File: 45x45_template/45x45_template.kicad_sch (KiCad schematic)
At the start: 10 parts, among them J1 Screw_Terminal_01x02

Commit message: Updated template.
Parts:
- removed J1: Screw_Terminal_01x02, TerminalBlock_Phoenix:TerminalBlock_Phoenix_MKDS-1,5-2-5.08_1x02_P5.08mm_Horizontal, symbol Connector:Screw_Terminal_01x02
- removed R3, R4: 100k, Resistor_THT:R_Axial_DIN0207_L6.3mm_D2.5mm_P15.24mm_Horizontal, symbol Device:R
- removed V1: VPULSE, symbol Simulation_SPICE:VPULSE
- added C1, C2: 100u, Capacitor_THT:CP_Radial_D8.0mm_P3.50mm, symbol Device:C_Polarized_US
- added J2: Screw_Terminal_01x02, TerminalBlock_Phoenix:TerminalBlock_Phoenix_MKDS-1,5-2-5.08_1x02_P5.08mm_Horizontal, symbol Connector:Screw_Terminal_01x02
- added SW1, SW2: SW_Push, Button_Switch_THT:SW_PUSH_6mm_H4.3mm, symbol Switch:SW_Push
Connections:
- net 0: now also C2.1, J2.2 (Pin_2), SW2.1; no longer R1.2
- net 9V: no longer names the net of R2.1
- net 9V: now also SW2.2
- net out: no longer names the net of R1.1
- net out: now also SW1.2; no longer R2.2
- new net: C1.2, C2.2
- new net Input voltage: J2.1 (Pin_1), SW1.1
- new net Output voltage: C1.1, R1.2, R2.2
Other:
- note added: "Kondenzator"
- note added: "Konektor za napajanje"
- note added: "Putanja za pražnjenje"
- note added: "Putanja za punjenje"
- note added: "Rupe za montiranje"
- note removed: "Dodaj Logo"
- note removed: "Dodaj OpenSans"
- title: (none) -> Redna i paralelna otpornost
- moved on the sheet: H1, H2, H3, H4

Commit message: Library updates.
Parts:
- added R3: ~, PEP_library:R_Axial_DIN0207_L6.3mm_D2.5mm_P15.24mm_Horizontal, symbol PEP_library:R_THT
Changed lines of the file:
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@@
+	)
+	(symbol
+		(lib_id "PEP_library:R_THT")
+		(at 97.79 83.82 0)
+		(unit 1)
+		(exclude_from_sim no)
+		(in_bom yes)
+		(on_board yes)
+		(dnp no)
+		(fields_autoplaced yes)
+		(property "Reference" "R3"
+			(at 100.33 81.9149 0)
+			(effects
+				(font
+					(size 1.27 1.27)
+				)
+				(justify left)
+			)
+		)
+		(property "Value" "~"
+			(at 100.33 83.82 0)
+			(effects
+				(font
+					(size 1.27 1.27)
+				)
+				(justify left)
+			)
+		)
+		(property "Footprint" "PEP_library:R_Axial_DIN0207_L6.3mm_D2.5mm_P15.24mm_Horizontal"
+			(at 97.79 87.122 0)
+			(effects
+				(font
+					(size 1.27 1.27)
+				)
+				(hide yes)
+			)
+		)
+		(property "Datasheet" ""
+			(at 97.79 83.82 0)
+			(effects
+				(font
+					(size 1.27 1.27)
+				)
+				(hide yes)
+			)
+		)
+		(property "Description" ""
+			(at 97.79 83.82 0)
+			(effects
+				(font
+					(size 1.27 1.27)
+				)
+				(hide yes)
+			)
+		)
+		(property "Size" "THT"
+			(at 100.33 85.7249 0)
+			(effects
+				(font
+					(size 1.27 1.27)
+				)
+				(justify left)
+			)
+		)
+		(property "Power rating" ""
+			(at 97.79 83.82 0)
+			(effects
+				(font
+					(size 1.27 1.27)
+				)
+				(hide yes)
+			)
+		)
+		(pin "2"
+		)
+		(pin "1"
+		)
+		(instances
+			(project ""
+				(path "/4bec5ddf-adbf-41fb-a069-c7630bb0044a"
+					(reference "R3")
+					(unit 1)
+				)
+			)
+		)
 	)
 	(symbol

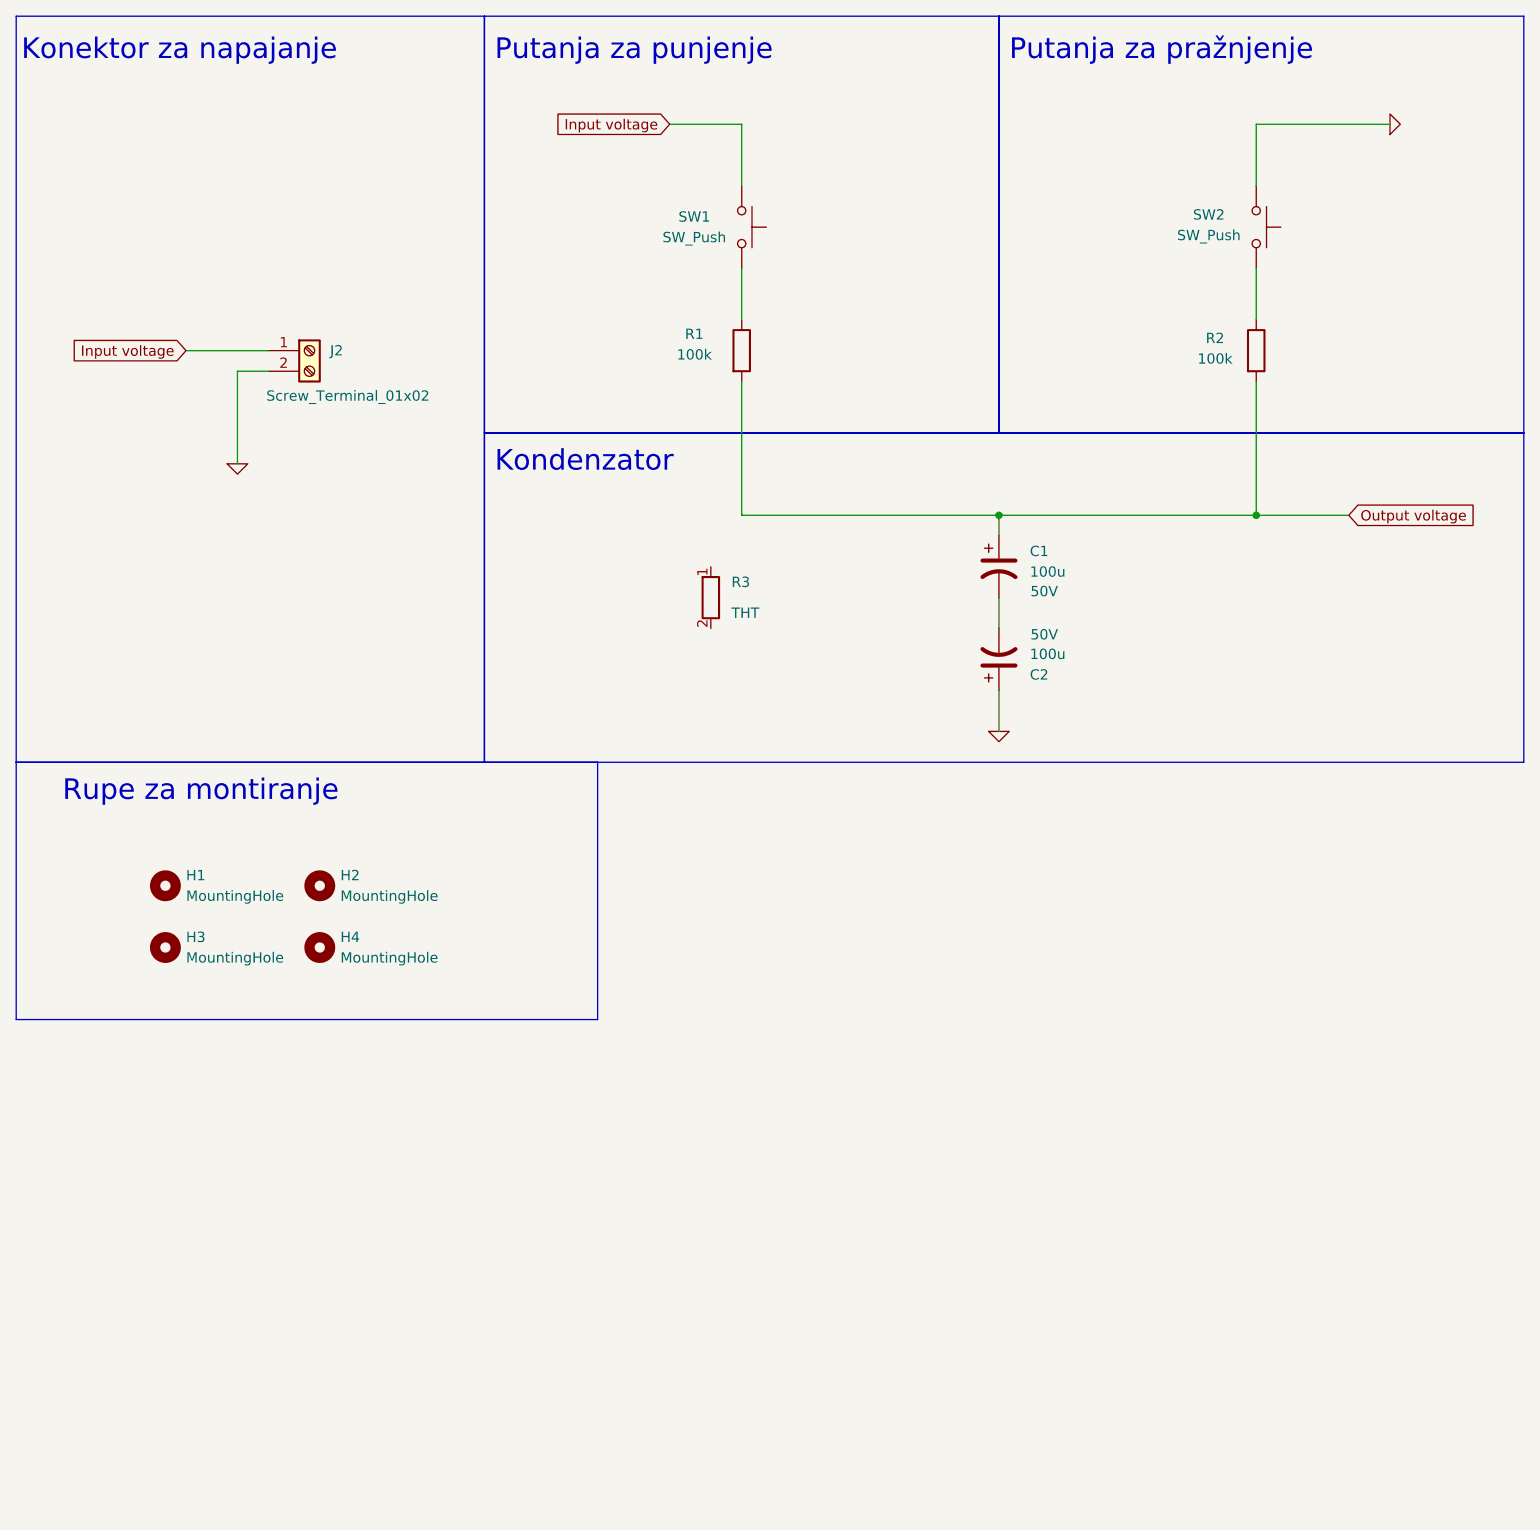
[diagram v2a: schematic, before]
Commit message: Template, library and PEP7 update.
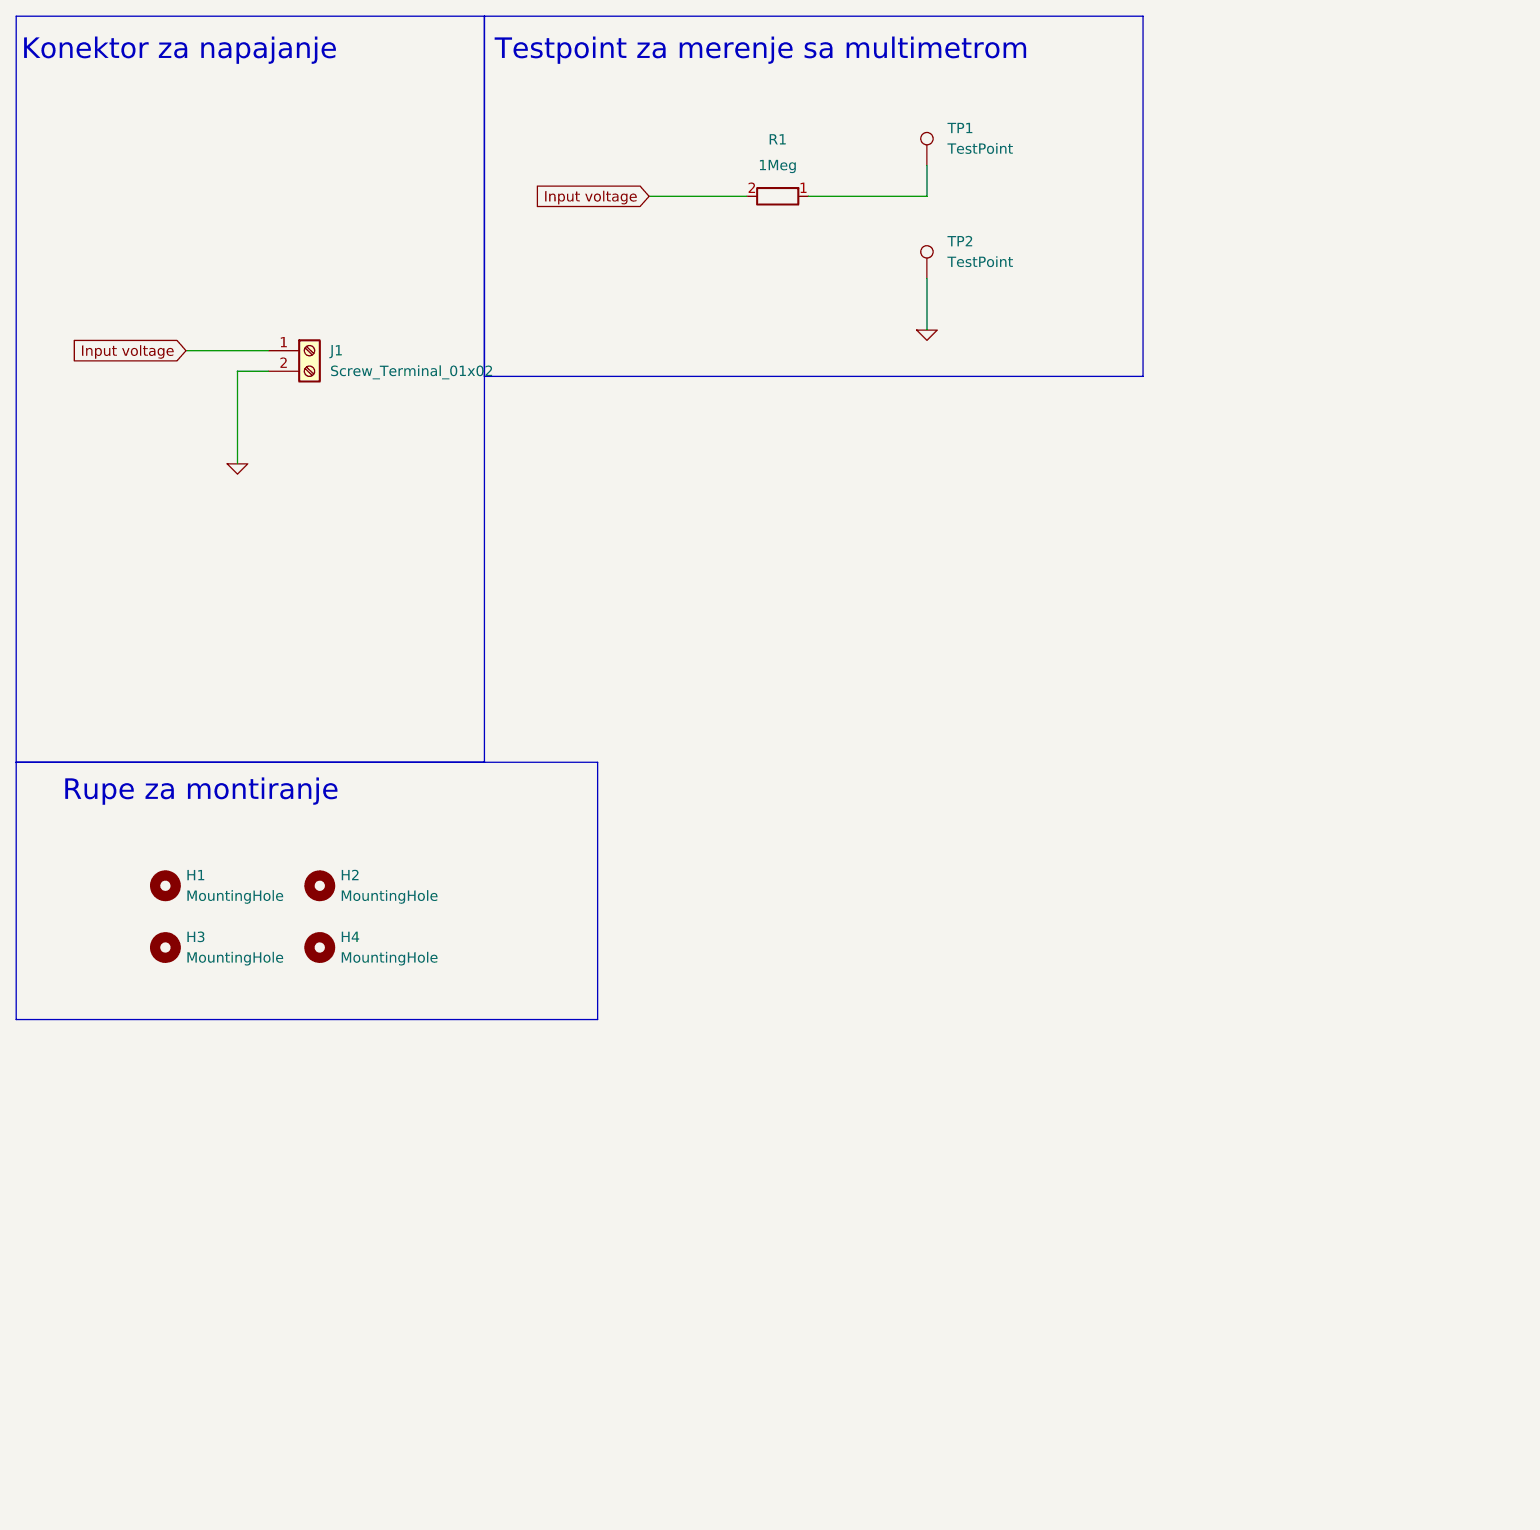
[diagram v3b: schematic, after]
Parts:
- removed C1, C2: 100u, Capacitor_THT:CP_Radial_D8.0mm_P3.50mm, symbol Device:C_Polarized_US
- removed J2: Screw_Terminal_01x02, TerminalBlock_Phoenix:TerminalBlock_Phoenix_MKDS-1,5-2-5.08_1x02_P5.08mm_Horizontal, symbol Connector:Screw_Terminal_01x02
- removed R1, R2: 100k, Resistor_SMD:R_1206_3216Metric_Pad1.30x1.75mm_HandSolder, symbol Device:R
- removed R3: ~, PEP_library:R_Axial_DIN0207_L6.3mm_D2.5mm_P15.24mm_Horizontal, symbol PEP_library:R_THT
- removed SW1, SW2: SW_Push, Button_Switch_THT:SW_PUSH_6mm_H4.3mm, symbol Switch:SW_Push
- added J1: Screw_Terminal_01x02, PEP_library:TerminalBlock_Phoenix_MKDS-1,5-2-5.08_1x02_P5.08mm_Horizontal, symbol PEP_library:Screw_Terminal_01x02
- added R1: 1Meg, PEP_library:R_Axial_DIN0207_L6.3mm_D2.5mm_P15.24mm_Horizontal, symbol PEP_library:R_THT
- added TP1, TP2: TestPoint, symbol Connector:TestPoint
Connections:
- net 0: now also J1.2 (Pin_2), TP2.1
- net Input voltage: now also J1.1 (Pin_1), R1.2
- new net: R1.1, TP1.1
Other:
- note added: "Testpoint za merenje sa multimetrom"
- note removed: "Kondenzator"
- note removed: "Putanja za pražnjenje"
- note removed: "Putanja za punjenje"
- title: Redna i paralelna otpornost -> MegaOtpornik u vazduhu
